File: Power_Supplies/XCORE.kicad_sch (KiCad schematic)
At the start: 34 parts, among them J22 2171790001, J8 FTSH-110-01-F-DV-K, U12 XU316-1024-TQ128-I24, U13 Si5351A-B-GT, U14 W25Q64JVSSIQ (FLASH MEMORY), X1 FA-238 24.0000MB-C0 (CRYSTAL), X2 FA-238 24.0000MB-C0

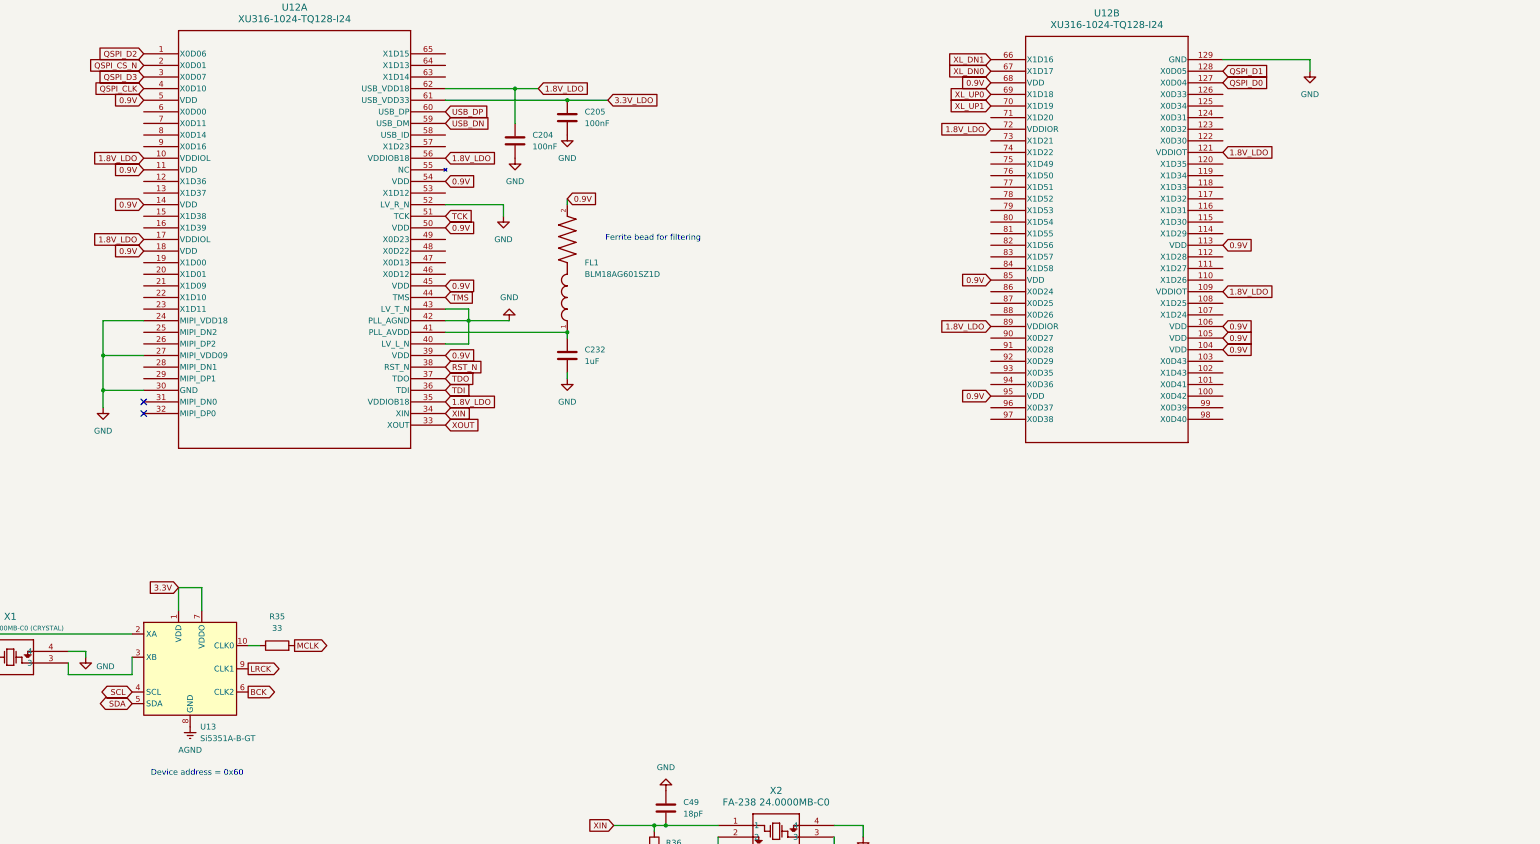
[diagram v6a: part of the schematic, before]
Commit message: Add files via upload
fixed voltage issues
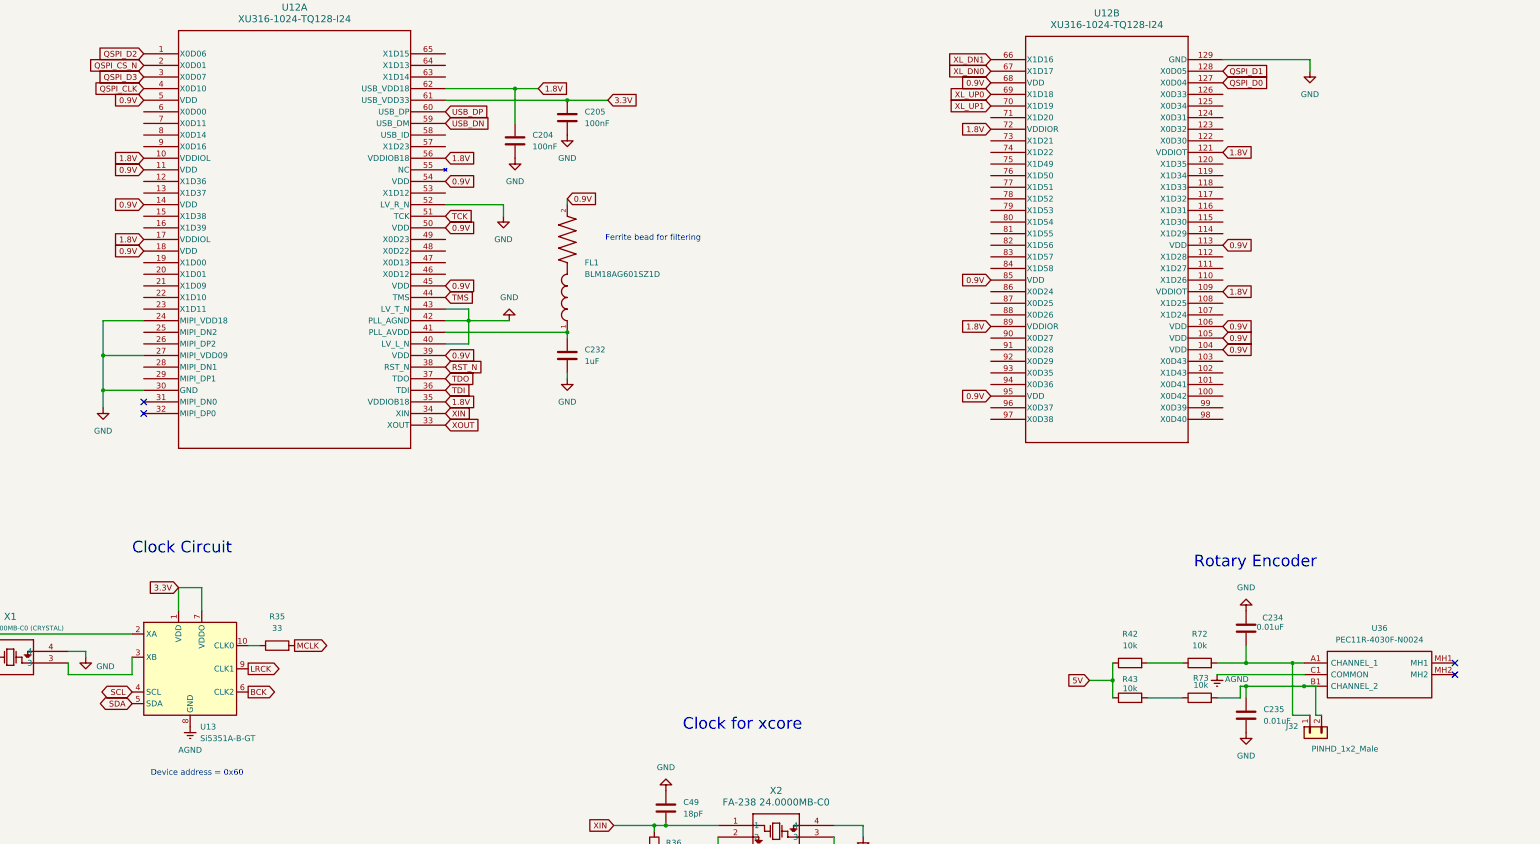
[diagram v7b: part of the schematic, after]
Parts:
- added C234, C235: 0.01uF, Capacitor_SMD:C_0402_1005Metric, symbol Device:C
- added J32: PINHD_1x2_Male, Connector_PinHeader_2.54mm:PinHeader_1x02_P2.54mm_Vertical, symbol PCM_SL_Pin_Headers:PINHD_1x2_Male
- added R42, R43, R72, R73: 10k, Resistor_SMD:R_0805_2012Metric, symbol Device:R
- added U36: PEC11R-4030F-N0024, SamacSys_Parts:PEC11R4030FN0024, symbol SamacSys_Parts:PEC11R-4030F-N0024
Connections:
- net 1.8V_LDO is gone; now on net 1.8V: C204.1, U12.10 (VDDIOL), U12.109 (VDDIOT), U12.121 (VDDIOT), U12.17 (VDDIOL), U12.35 (VDDIOB18), U12.56 (VDDIOB18), U12.62 (USB_VDD18), U12.72 (VDDIOR), U12.89 (VDDIOR)
- net 3.3V_LDO is gone; now on net 3.3V: C205.1, U12.61 (USB_VDD33)
- net AGND: now also U36.C1 (COMMON)
- net GND: now also C234.1, C235.2
- new net: C235.1, J32.2, R73.2, U36.B1 (CHANNEL_2)
- new net: C234.2, J32.1, R72.2, U36.A1 (CHANNEL_1)
- new net: R42.2, R72.1
- new net: R43.2, R73.1
- new net 5V: R42.1, R43.1
- no-connect marks 3 -> 5
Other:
- note added: "Clock Circuit"
- note added: "Clock for xcore"
- note added: "Rotary Encoder"

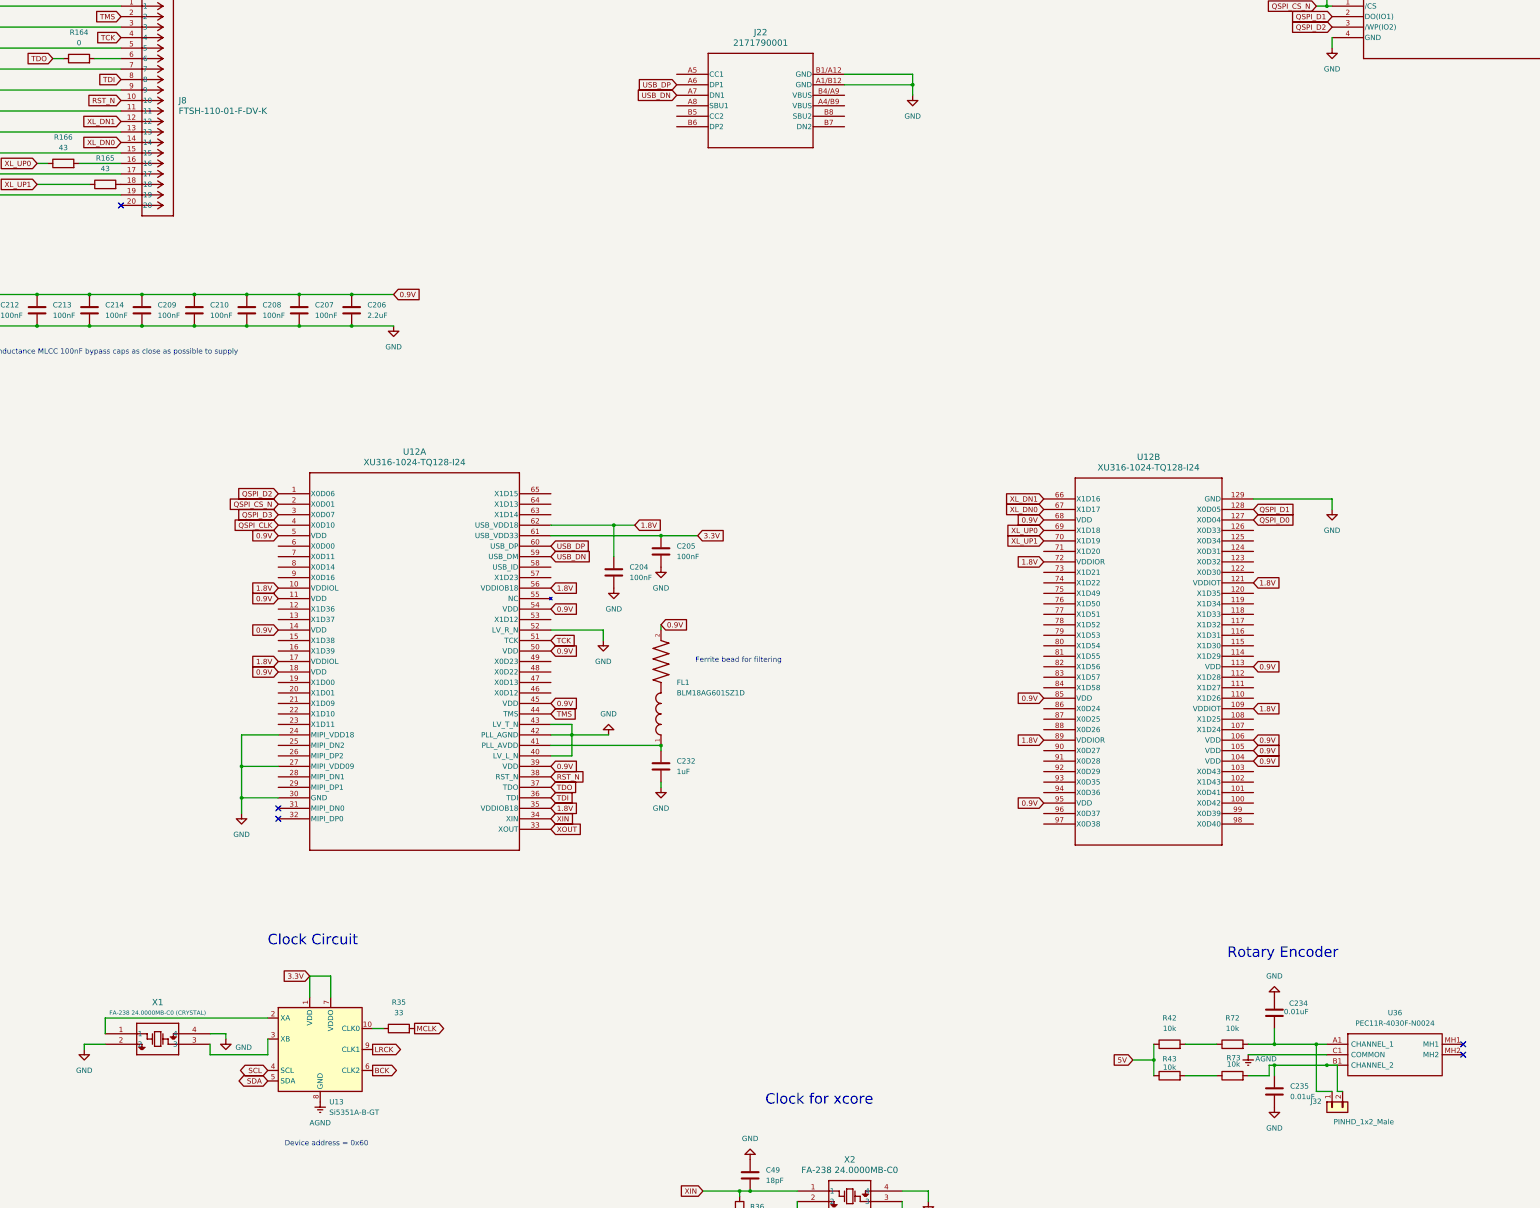
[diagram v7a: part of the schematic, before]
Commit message: connected ADC/DACs, USB
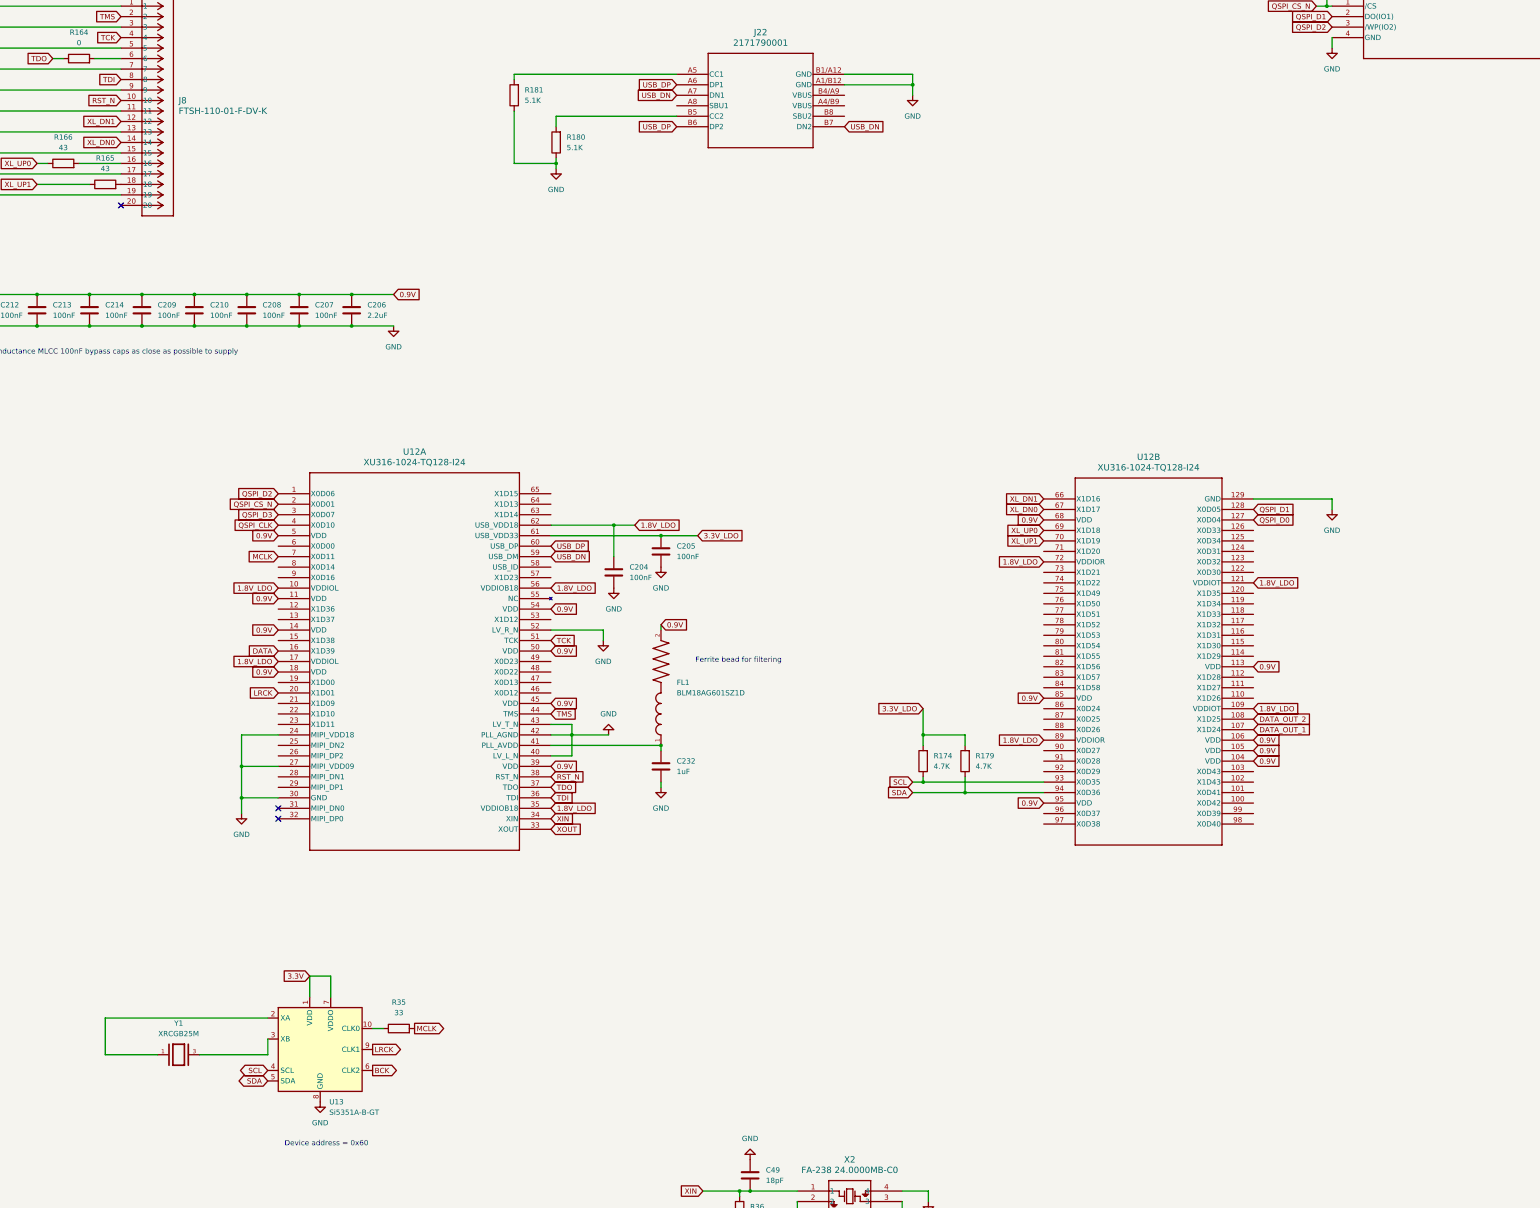
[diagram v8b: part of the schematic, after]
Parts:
- removed C234, C235: 0.01uF, Capacitor_SMD:C_0402_1005Metric, symbol Device:C
- removed J32: PINHD_1x2_Male, Connector_PinHeader_2.54mm:PinHeader_1x02_P2.54mm_Vertical, symbol PCM_SL_Pin_Headers:PINHD_1x2_Male
- removed R42, R43, R72, R73: 10k, Resistor_SMD:R_0805_2012Metric, symbol Device:R
- removed U36: PEC11R-4030F-N0024, SamacSys_Parts:PEC11R4030FN0024, symbol SamacSys_Parts:PEC11R-4030F-N0024
- removed X1: FA-238 24.0000MB-C0 (CRYSTAL), SamacSys_Parts:FA-238_EPS, symbol SDLibrary:FA-238_24.0000MB-C0
- added R174, R179: 4.7K, Resistor_SMD:R_0805_2012Metric, symbol Device:R
- added R180, R181: 5.1K, Resistor_SMD:R_0805_2012Metric, symbol Device:R
- added Y1: XRCGB25M, XRCGB25M, symbol SDLibrary:XRCGB25M000F3A00R0
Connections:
- net AGND is gone; now on net GND: U13.8 (GND)
- net 1.8V: no longer C204.1, U12.10 (VDDIOL), U12.109 (VDDIOT), U12.121 (VDDIOT), U12.17 (VDDIOL), U12.35 (VDDIOB18), U12.56 (VDDIOB18), U12.62 (USB_VDD18), U12.72 (VDDIOR), U12.89 (VDDIOR)
- net 3.3V: no longer C205.1, U12.61 (USB_VDD33)
- net GND: now also R180.1, R181.1
- net LRCK: now also U12.20 (X1D01)
- net MCLK: now also U12.7 (X0D11)
- net SCL: now also U12.93 (X0D35), R174.1
- net SDA: now also U12.94 (X0D36), R179.1
- net USB_DN: now also J22.B7 (DN2)
- net USB_DP: now also J22.B6 (DP2)
- net DATA_OUT_1: now reaches U12.107 (X1D24)
- net DATA_OUT_2: now reaches U12.108 (X1D25)
- net at U13.2 (XA): now also Y1.1
- net at U13.3 (XB): now also Y1.3
- net at J22.A5 (CC1): now also R181.2
- net at J22.B5 (CC2): now also R180.2
- net DATA: now reaches U12.16 (X1D39)
- new net 1.8V_LDO: C204.1, U12.10 (VDDIOL), U12.109 (VDDIOT), U12.121 (VDDIOT), U12.17 (VDDIOL), U12.35 (VDDIOB18), U12.56 (VDDIOB18), U12.62 (USB_VDD18), U12.72 (VDDIOR), U12.89 (VDDIOR)
- new net 3.3V_LDO: C205.1, R174.2, R179.2, U12.61 (USB_VDD33)
- no-connect marks 5 -> 3
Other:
- note removed: "Clock Circuit"
- note removed: "Clock for xcore"
- note removed: "Rotary Encoder"
